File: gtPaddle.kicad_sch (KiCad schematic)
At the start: 34 parts, among them IC1 74157N, IC2 74157N, J1 Conn_01x02_Pin, J2 Conn_01x02_Pin, J3 Conn_01x02_Pin, J4 Conn_01x02_Pin, Q1 2N3904, Q10 2N3904, Q9 2N3904, U1 ADC0804LCN

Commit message: added soldered jumpers bridged and unbridged to handle optional setups
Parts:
- added JP2, JP3: SolderJumper_2_Open, symbol Jumper:SolderJumper_2_Open
- added JP4, JP5: SolderJumper_2_Bridged, symbol Jumper:SolderJumper_2_Bridged
- added Q2, Q3: 2N3904, Package_TO_SOT_THT:TO-92_Inline, symbol Transistor_BJT:2N3904
- added R18, R21: 10K, gpad1:0207_10, symbol gpad1-eagle-import:R-US_0207/10
- added R19, R20: 3.3K, gpad1:0207_10, symbol gpad1-eagle-import:R-US_0207/10
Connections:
- net VCC: now also R19.1, R20.1
- net at Q10.1 (E), Q9.1 (E): now also JP2.1 (A)
- net at IC2.4 (1Y): now also JP4.1 (A); no longer JP1.1
- net at JP1.2: now also JP5.2 (B); no longer IC2.7 (2Y)
- new net: JP3.1 (A), Q2.1 (E), Q3.1 (E)
- new net: Q3.2 (B), R21.2
- new net: Q3.3 (C), R20.2
- new net: Q2.3 (C), R19.2
- new net: JP1.1, JP4.2 (B)
- new net: IC2.7 (2Y), JP5.1 (A)
- new net: Q2.2 (B), R18.2
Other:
- moved on the sheet: Q10, Q9, R14, R15, R16, R17, R5, R6, R7, R8

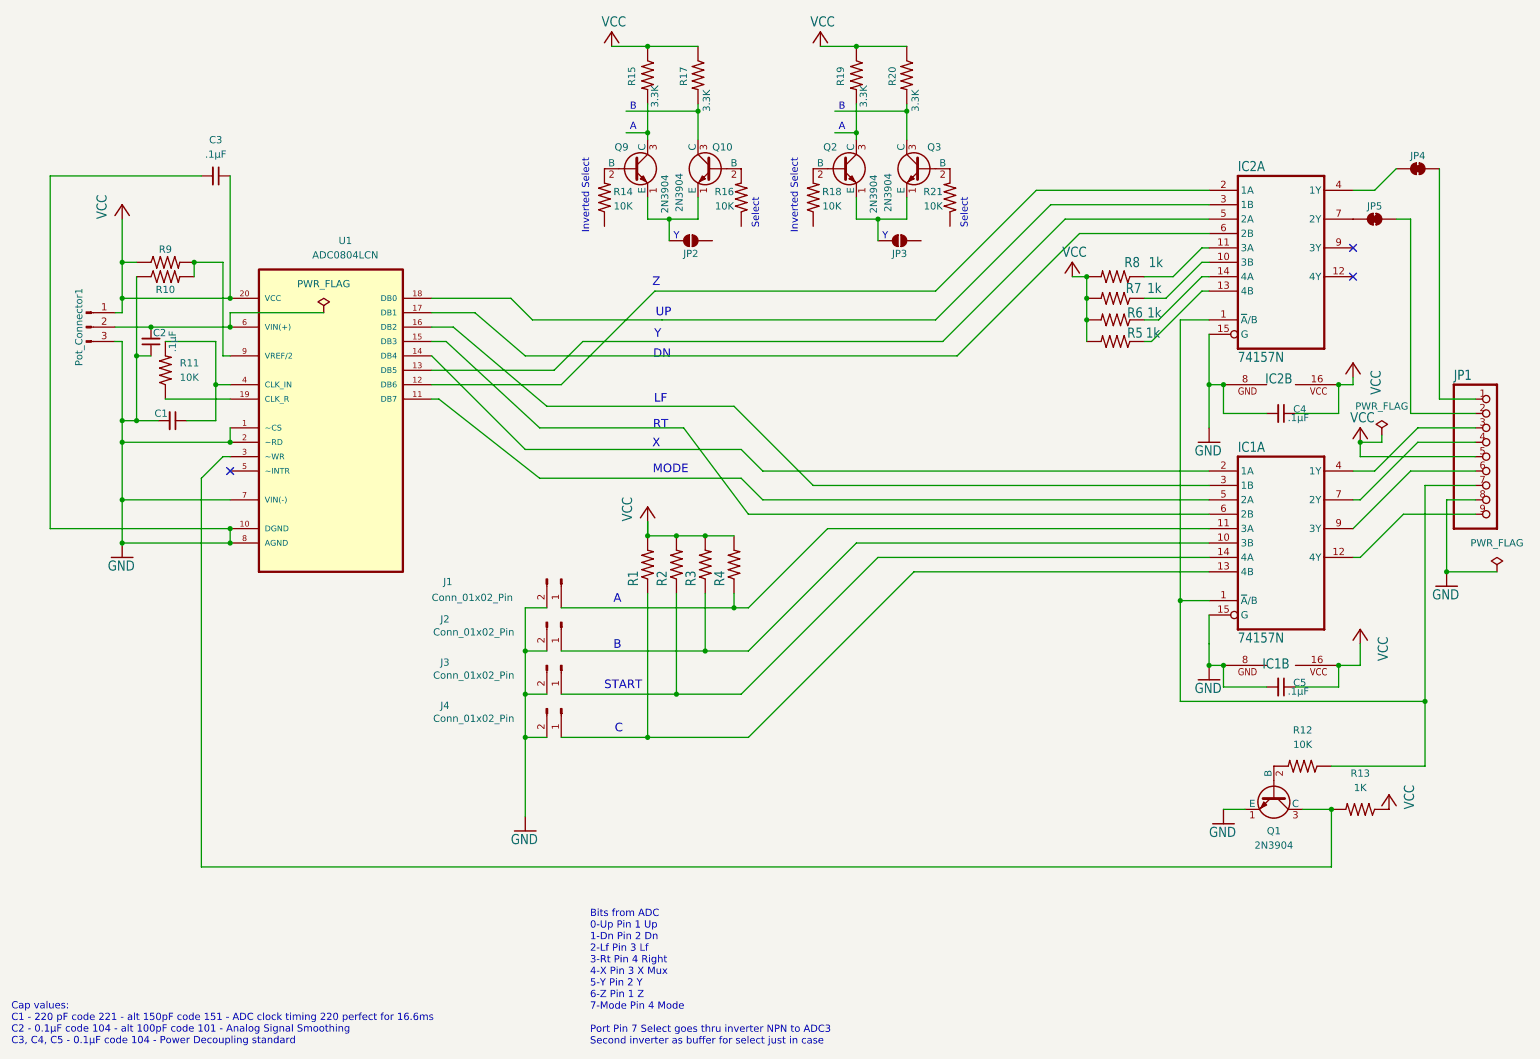
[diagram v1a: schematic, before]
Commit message: dual npn mux option added to schematic
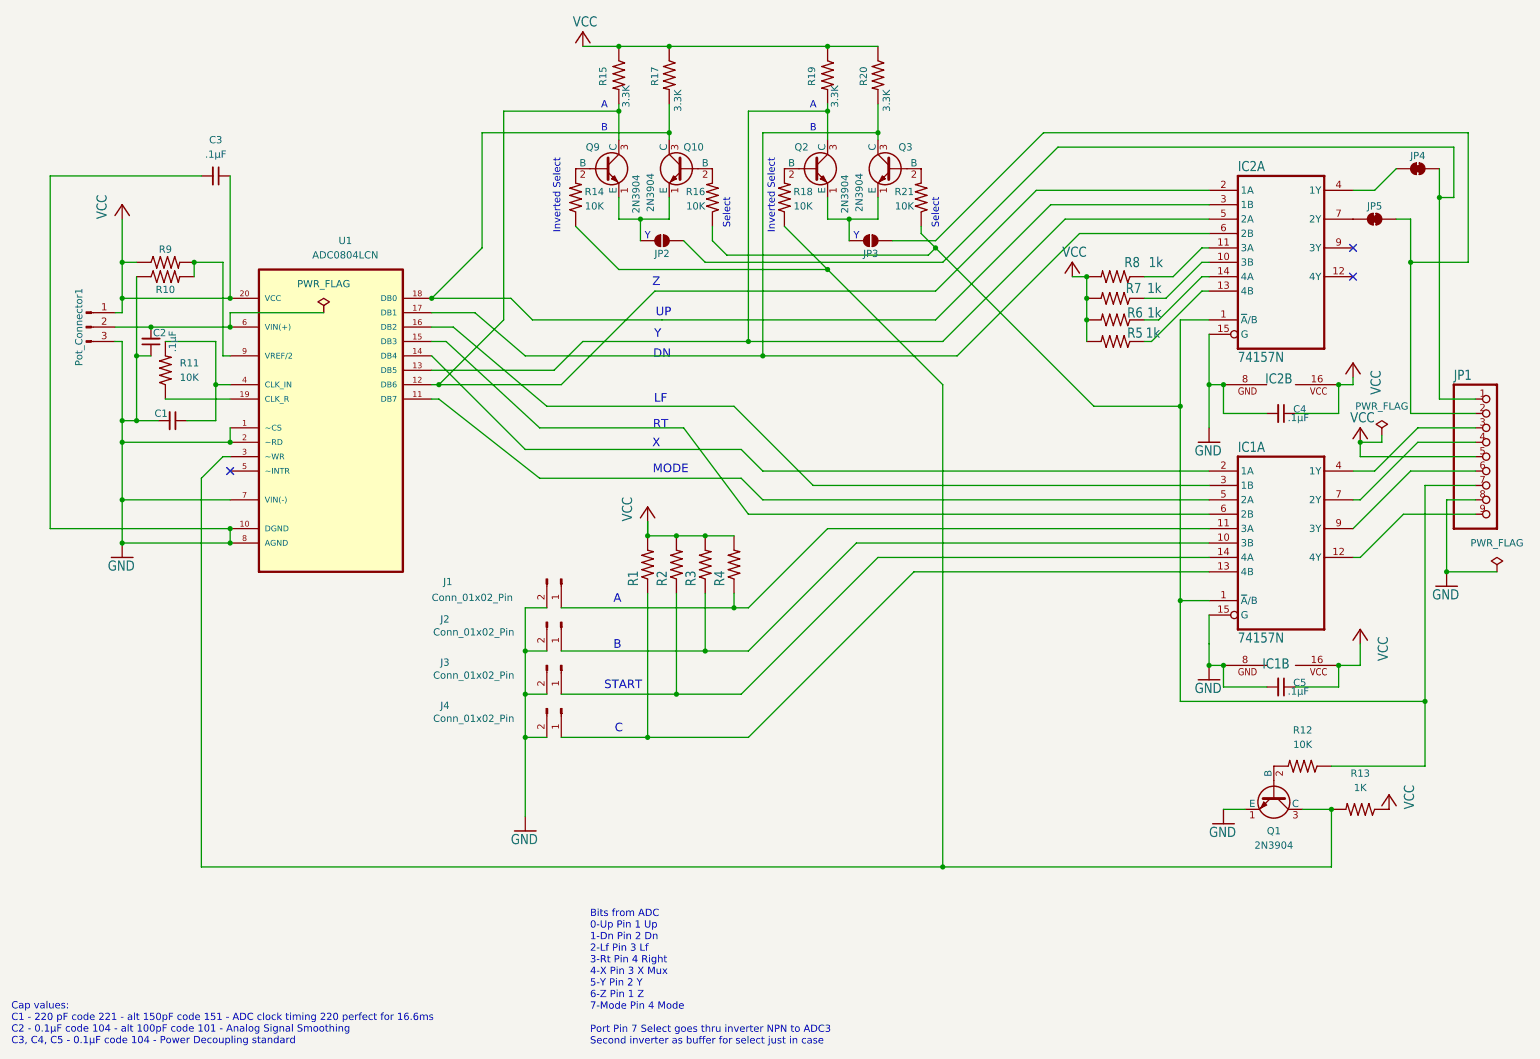
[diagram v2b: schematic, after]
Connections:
- net at Q1.3 (C), R13.2, U1.3 (~WR): now also R14.1, R18.1
- net at Q9.3 (C), R15.2: now also IC2.2 (1A), U1.12 (DB6)
- net at Q3.3 (C), R20.2: now also IC2.6 (2B), U1.17 (DB1)
- net at Q10.3 (C), R17.2: now also IC2.3 (1B), U1.18 (DB0)
- net at R21.1: now also IC1.1 (~{A}/B), IC2.1 (~{A}/B), JP1.7, R12.1, R16.1
- net at Q2.3 (C), R19.2: now also IC2.5 (2A), U1.13 (DB5)
- net at JP1.1, JP4.2 (B): now also JP2.2 (B)
- net at JP1.2, JP5.2 (B): now also JP3.2 (B)
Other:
- moved on the sheet: JP2, JP3, Q10, Q2, Q3, Q9, R14, R15, R16, R17, R18, R19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

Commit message: footprint assignments
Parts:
- J1, J2, J3, J4: footprint (none) -> Connector_JST:JST_PH_B2B-PH-K_1x02_P2.00mm_Vertical
- JP2, JP3: footprint (none) -> Jumper:SolderJumper-2_P1.3mm_Open_RoundedPad1.0x1.5mm
- JP4, JP5: footprint (none) -> Jumper:SolderJumper-2_P1.3mm_Bridged_RoundedPad1.0x1.5mm
- Pot_Connector1: footprint Connector_JST:JST_ACH_BM02B-ACHSS-GAN-ETF_1x02-1MP_P1.20mm_Vertical -> Connector_JST:JST_PH_B3B-PH-K_1x03_P2.00mm_Vertical
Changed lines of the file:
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@@
 			)
 		)
-		(property "Footprint" ""
+		(property "Footprint" "Connector_JST:JST_PH_B2B-PH-K_1x02_P2.00mm_Vertical"
 			(at 116.84 135.89 0)
 			(effects
@@
 			)
 		)
-		(property "Footprint" ""
+		(property "Footprint" "Connector_JST:JST_PH_B2B-PH-K_1x02_P2.00mm_Vertical"
 			(at 116.84 128.27 0)
 			(effects
@@
 			)
 		)
-		(property "Footprint" ""
+		(property "Footprint" "Connector_JST:JST_PH_B2B-PH-K_1x02_P2.00mm_Vertical"
 			(at 116.84 113.03 0)
 			(effects
@@
 			)
 		)
-		(property "Footprint" ""
+		(property "Footprint" "Jumper:SolderJumper-2_P1.3mm_Bridged_RoundedPad1.0x1.5mm"
 			(at 267.97 40.64 0)
 			(effects
@@
 			)
 		)
-		(property "Footprint" ""
+		(property "Footprint" "Jumper:SolderJumper-2_P1.3mm_Open_RoundedPad1.0x1.5mm"
 			(at 134.62 53.34 0)
 			(effects
@@
 			)
 		)
-		(property "Footprint" ""
+		(property "Footprint" "Connector_JST:JST_PH_B2B-PH-K_1x02_P2.00mm_Vertical"
 			(at 116.84 120.65 0)
 			(effects
@@
 			)
 		)
-		(property "Footprint" "Connector_JST:JST_ACH_BM02B-ACHSS-GAN-ETF_1x02-1MP_P1.20mm_Vertical"
+		(property "Footprint" "Connector_JST:JST_PH_B3B-PH-K_1x03_P2.00mm_Vertical"
 			(at 33.02 68.58 0)
 			(effects
@@
 			)
 		)
-		(property "Footprint" ""
+		(property "Footprint" "Jumper:SolderJumper-2_P1.3mm_Bridged_RoundedPad1.0x1.5mm"
 			(at 260.35 49.53 0)
 			(effects
@@
 			)
 		)
-		(property "Footprint" ""
+		(property "Footprint" "Jumper:SolderJumper-2_P1.3mm_Open_RoundedPad1.0x1.5mm"
 			(at 171.45 53.34 0)
 			(effects

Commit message: first pass placement no traces
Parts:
- C1, C2, C3, C4, C5: footprint Capacitor_THT:CP_Radial_D4.0mm_P1.50mm -> Capacitor_THT:C_Disc_D3.8mm_W2.6mm_P2.50mm
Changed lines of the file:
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@@
 			)
 		)
-		(property "Footprint" "Capacitor_THT:CP_Radial_D4.0mm_P1.50mm"
+		(property "Footprint" "Capacitor_THT:C_Disc_D3.8mm_W2.6mm_P2.50mm"
 			(at 243.84 83.82 0)
 			(effects
@@
 			)
 		)
-		(property "Footprint" "Capacitor_THT:CP_Radial_D4.0mm_P1.50mm"
+		(property "Footprint" "Capacitor_THT:C_Disc_D3.8mm_W2.6mm_P2.50mm"
 			(at 48.26 85.09 0)
 			(effects
@@
 			)
 		)
-		(property "Footprint" "Capacitor_THT:CP_Radial_D4.0mm_P1.50mm"
+		(property "Footprint" "Capacitor_THT:C_Disc_D3.8mm_W2.6mm_P2.50mm"
 			(at 243.84 132.08 0)
 			(effects
@@
 			)
 		)
-		(property "Footprint" "Capacitor_THT:CP_Radial_D4.0mm_P1.50mm"
+		(property "Footprint" "Capacitor_THT:C_Disc_D3.8mm_W2.6mm_P2.50mm"
 			(at 44.45 71.12 0)
 			(effects
@@
 			)
 		)
-		(property "Footprint" "Capacitor_THT:CP_Radial_D4.0mm_P1.50mm"
+		(property "Footprint" "Capacitor_THT:C_Disc_D3.8mm_W2.6mm_P2.50mm"
 			(at 55.88 41.91 0)
 			(effects

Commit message: tighter layout
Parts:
- R1, R10, R11, R12, R13, R14, R15, R16, R17, R18, R19, R2, R20, R21, R3, R4, R5, R6, R7, R8, R9: footprint gpad1:0207_10 -> Resistor_THT:R_Axial_DIN0309_L9.0mm_D3.2mm_P2.54mm_Vertical
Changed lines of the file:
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@@
 			)
 		)
-		(property "Footprint" "gpad1:0207_10"
+		(property "Footprint" "Resistor_THT:R_Axial_DIN0309_L9.0mm_D3.2mm_P2.54mm_Vertical"
 			(at 46.99 57.15 0)
 			(effects
@@
 			)
 		)
-		(property "Footprint" "gpad1:0207_10"
+		(property "Footprint" "Resistor_THT:R_Axial_DIN0309_L9.0mm_D3.2mm_P2.54mm_Vertical"
 			(at 214.63 59.69 0)
 			(effects
@@
 			)
 		)
-		(property "Footprint" "gpad1:0207_10"
+		(property "Footprint" "Resistor_THT:R_Axial_DIN0309_L9.0mm_D3.2mm_P2.54mm_Vertical"
 			(at 257.81 153.67 0)
 			(effects
@@
 			)
 		)
-		(property "Footprint" "gpad1:0207_10"
+		(property "Footprint" "Resistor_THT:R_Axial_DIN0309_L9.0mm_D3.2mm_P2.54mm_Vertical"
 			(at 127 24.13 0)
 			(effects
@@
 			)
 		)
-		(property "Footprint" "gpad1:0207_10"
+		(property "Footprint" "Resistor_THT:R_Axial_DIN0309_L9.0mm_D3.2mm_P2.54mm_Vertical"
 			(at 214.63 67.31 0)
 			(effects
@@
 			)
 		)
-		(property "Footprint" "gpad1:0207_10"
+		(property "Footprint" "Resistor_THT:R_Axial_DIN0309_L9.0mm_D3.2mm_P2.54mm_Vertical"
 			(at 180.34 45.72 0)
 			(effects
@@
 			)
 		)
-		(property "Footprint" "gpad1:0207_10"
+		(property "Footprint" "Resistor_THT:R_Axial_DIN0309_L9.0mm_D3.2mm_P2.54mm_Vertical"
 			(at 137.16 110.49 0)
 			(effects
@@
 			)
 		)
-		(property "Footprint" "gpad1:0207_10"
+		(property "Footprint" "Resistor_THT:R_Axial_DIN0309_L9.0mm_D3.2mm_P2.54mm_Vertical"
 			(at 46.99 76.2 0)
 			(effects
@@
 			)
 		)
-		(property "Footprint" "gpad1:0207_10"
+		(property "Footprint" "Resistor_THT:R_Axial_DIN0309_L9.0mm_D3.2mm_P2.54mm_Vertical"
 			(at 163.83 24.13 0)
 			(effects
@@
 			)
 		)
-		(property "Footprint" "gpad1:0207_10"
+		(property "Footprint" "Resistor_THT:R_Axial_DIN0309_L9.0mm_D3.2mm_P2.54mm_Vertical"
 			(at 119.38 45.72 0)
 			(effects
@@
 			)
 		)
-		(property "Footprint" "gpad1:0207_10"
+		(property "Footprint" "Resistor_THT:R_Axial_DIN0309_L9.0mm_D3.2mm_P2.54mm_Vertical"
 			(at 247.65 146.05 0)
 			(effects
@@
 			)
 		)
-		(property "Footprint" "gpad1:0207_10"
+		(property "Footprint" "Resistor_THT:R_Axial_DIN0309_L9.0mm_D3.2mm_P2.54mm_Vertical"
 			(at 46.99 59.69 0)
 			(effects
@@
 			)
 		)
-		(property "Footprint" "gpad1:0207_10"
+		(property "Footprint" "Resistor_THT:R_Axial_DIN0309_L9.0mm_D3.2mm_P2.54mm_Vertical"
 			(at 143.51 45.72 0)
 			(effects
@@
 			)
 		)
-		(property "Footprint" "gpad1:0207_10"
+		(property "Footprint" "Resistor_THT:R_Axial_DIN0309_L9.0mm_D3.2mm_P2.54mm_Vertical"
 			(at 214.63 71.12 0)
 			(effects
@@
 			)
 		)
-		(property "Footprint" "gpad1:0207_10"
+		(property "Footprint" "Resistor_THT:R_Axial_DIN0309_L9.0mm_D3.2mm_P2.54mm_Vertical"
 			(at 132.08 110.49 0)
 			(effects
@@
 			)
 		)
-		(property "Footprint" "gpad1:0207_10"
+		(property "Footprint" "Resistor_THT:R_Axial_DIN0309_L9.0mm_D3.2mm_P2.54mm_Vertical"
 			(at 214.63 63.5 0)
 			(effects
@@
 			)
 		)
-		(property "Footprint" "gpad1:0207_10"
+		(property "Footprint" "Resistor_THT:R_Axial_DIN0309_L9.0mm_D3.2mm_P2.54mm_Vertical"
 			(at 147.32 110.49 0)
 			(effects
@@
 			)
 		)
-		(property "Footprint" "gpad1:0207_10"
+		(property "Footprint" "Resistor_THT:R_Axial_DIN0309_L9.0mm_D3.2mm_P2.54mm_Vertical"
 			(at 156.21 45.72 0)
 			(effects
@@
 			)
 		)
-		(property "Footprint" "gpad1:0207_10"
+		(property "Footprint" "Resistor_THT:R_Axial_DIN0309_L9.0mm_D3.2mm_P2.54mm_Vertical"
 			(at 135.89 24.13 0)
 			(effects
@@
 			)
 		)
-		(property "Footprint" "gpad1:0207_10"
+		(property "Footprint" "Resistor_THT:R_Axial_DIN0309_L9.0mm_D3.2mm_P2.54mm_Vertical"
 			(at 172.72 24.13 0)
 			(effects
@@
 			)
 		)
-		(property "Footprint" "gpad1:0207_10"
+		(property "Footprint" "Resistor_THT:R_Axial_DIN0309_L9.0mm_D3.2mm_P2.54mm_Vertical"
 			(at 142.24 110.49 0)
 			(effects

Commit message: edited bjt footprint
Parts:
- Q1, Q10, Q2, Q3, Q9: footprint Package_TO_SOT_THT:TO-92_Inline -> Package_TO_SOT_THT:TO-92S-EBC
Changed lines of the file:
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@@
 			)
 		)
-		(property "Footprint" "Package_TO_SOT_THT:TO-92_Inline"
+		(property "Footprint" "Package_TO_SOT_THT:TO-92S-EBC"
 			(at 170.18 42.545 0)
 			(effects
@@
 			)
 		)
-		(property "Footprint" "Package_TO_SOT_THT:TO-92_Inline"
+		(property "Footprint" "Package_TO_SOT_THT:TO-92S-EBC"
 			(at 133.35 42.545 0)
 			(effects
@@
 			)
 		)
-		(property "Footprint" "Package_TO_SOT_THT:TO-92_Inline"
+		(property "Footprint" "Package_TO_SOT_THT:TO-92S-EBC"
 			(at 129.54 42.545 0)
 			(effects
@@
 			)
 		)
-		(property "Footprint" "Package_TO_SOT_THT:TO-92_Inline"
+		(property "Footprint" "Package_TO_SOT_THT:TO-92S-EBC"
 			(at 240.665 156.21 0)
 			(effects
@@
 			)
 		)
-		(property "Footprint" "Package_TO_SOT_THT:TO-92_Inline"
+		(property "Footprint" "Package_TO_SOT_THT:TO-92S-EBC"
 			(at 166.37 42.545 0)
 			(effects

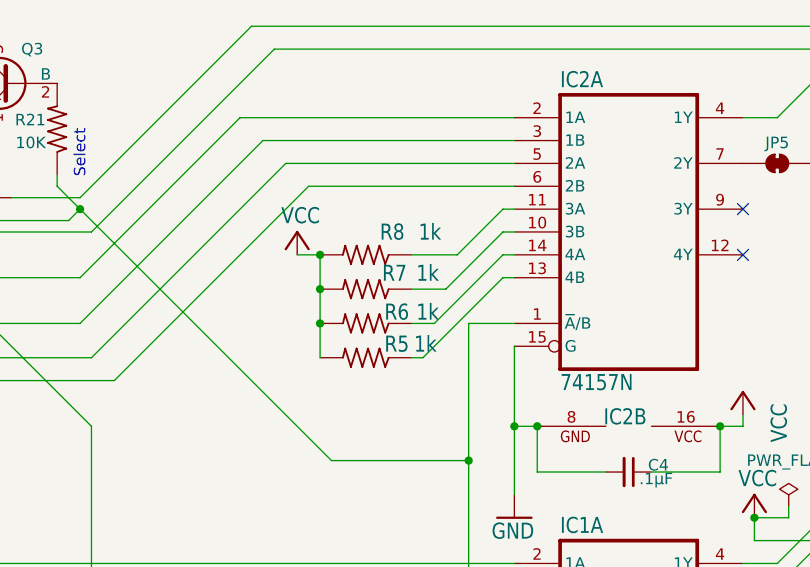
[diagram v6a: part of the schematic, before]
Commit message: ground unused mux pins
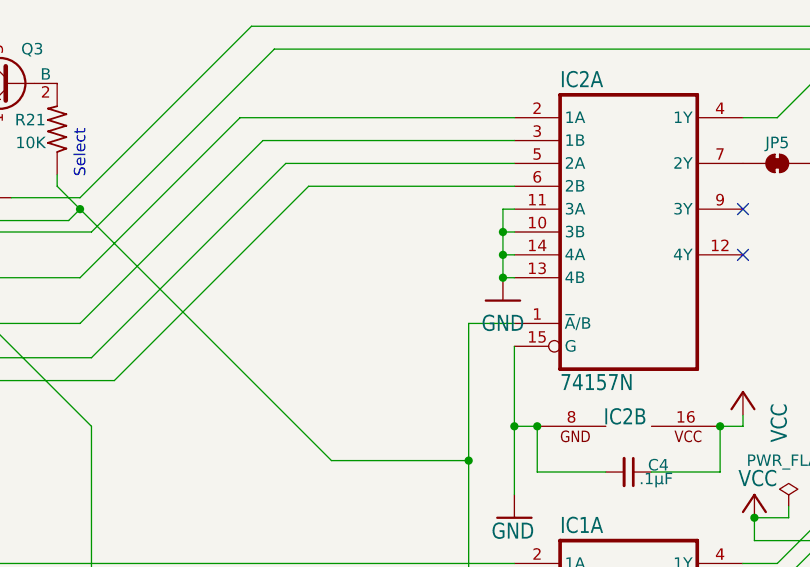
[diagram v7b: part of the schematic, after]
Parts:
- removed R5, R6, R7, R8: 1k, Resistor_THT:R_Axial_DIN0309_L9.0mm_D3.2mm_P2.54mm_Vertical, symbol gpad1-eagle-import:R-US_0207/10
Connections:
- net GND: now also IC2.10 (3B), IC2.11 (3A), IC2.13 (4B), IC2.14 (4A)

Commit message: remove npn muxes
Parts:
- removed JP2, JP3: SolderJumper_2_Open, Jumper:SolderJumper-2_P1.3mm_Open_RoundedPad1.0x1.5mm, symbol Jumper:SolderJumper_2_Open
- removed JP4, JP5: SolderJumper_2_Bridged, Jumper:SolderJumper-2_P1.3mm_Bridged_RoundedPad1.0x1.5mm, symbol Jumper:SolderJumper_2_Bridged
- removed Q10, Q2, Q3, Q9: 2N3904, Package_TO_SOT_THT:TO-92S-EBC, symbol Transistor_BJT:2N3904
- removed R14, R16, R18, R21: 10K, Resistor_THT:R_Axial_DIN0309_L9.0mm_D3.2mm_P2.54mm_Vertical, symbol gpad1-eagle-import:R-US_0207/10
- removed R15, R17, R19, R20: 3.3K, Resistor_THT:R_Axial_DIN0309_L9.0mm_D3.2mm_P2.54mm_Vertical, symbol gpad1-eagle-import:R-US_0207/10
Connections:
- net at IC2.4 (1Y): now also JP1.1
- net at JP1.2: now also IC2.7 (2Y)
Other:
- note removed: "Inverted Select"
- note removed: "Select"
